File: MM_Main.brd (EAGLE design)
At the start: 101.4 x 83.6 mm, 73 parts, among them IC1 ULN2003AD, IC2 TB6612FNG, IC4 LD117ADT50TR, Q1 TEFT4300, Q2 TEFT4300, Q3 TEFT4300, Q4 TEFT4300, Q7 8MHz, U1 STM32F405RGT6

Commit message: dodalem stm32f4 do biblioteki
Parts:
- removed U$3: STM32F405/415_LQFP64, STM32F10x F4xx:STM32F405/415_LQFP64
- added U$6: STM32F4X5, _microMouse:STM32F4-LQFP64
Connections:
- net +3V3: now also U$6.VDDA, U$6.VDD_0, U$6.VDD_1, U$6.VDD_2, U$6.VDD_3; no longer U$3.VDDA, U$3.VDD_0, U$3.VDD_1, U$3.VDD_2, U$3.VDD_3
- net ADC_L: now also U$6.PC1; no longer U$3.PC1
- net ADC_LF: now also U$6.PC0; no longer U$3.PC0
- net ADC_R: now also U$6.PC2; no longer U$3.PC2
- net ADC_RF: now also U$6.PC3; no longer U$3.PC3
- net ADC_VBAT: now also U$6.PB1; no longer U$3.PB1
- net BOOT0: now also U$6.BOOT0; no longer U$3.BOOT0
- net BTN: now also U$6.PB0; no longer U$3.PB0
- net BT_RXD: now also U$6.PA9; no longer U$3.PA9
- net BT_TXD: now also U$6.PA10; no longer U$3.PA10
- net BUZZER: now also U$6.PA5; no longer U$3.PA5
- net CS_A: now also U$6.PB4; no longer U$3.PB4
- net CS_G: now also U$6.PB3; no longer U$3.PB3
- net D_L: now also U$6.PA2; no longer U$3.PA2
- net D_LF: now also U$6.PA1; no longer U$3.PA1
- net D_LL: now also U$6.PC13; no longer U$3.PC13
- net D_R: now also U$6.PA3; no longer U$3.PA3
- net D_RF: now also U$6.PA4; no longer U$3.PA4
- net D_RR: now also U$6.PC14; no longer U$3.PC14
- net ENCL_A: now also U$6.PA6; no longer U$3.PA6
- net ENCL_B: now also U$6.PA7; no longer U$3.PA7
- net ENCR_A: now also U$6.PB6; no longer U$3.PB6
- net ENCR_B: now also U$6.PB7; no longer U$3.PB7
- net GND: now also U$6.VSS_0, U$6.VSS_1; no longer U$3.VSS_0, U$3.VSS_1
- net GNDA: now also U$6.VSSA; no longer U$3.VSSA
- net INT_A: now also U$6.PB5; no longer U$3.PB5
- net LED1: now also U$6.PB9; no longer U$3.PB9
- net LED2: now also U$6.PB8; no longer U$3.PB8
- net MISO: now also U$6.PC11; no longer U$3.PC11
- net ML_IN1: now also U$6.PC6; no longer U$3.PC6
- net ML_IN2: now also U$6.PC7; no longer U$3.PC7
- net ML_PWM: now also U$6.PB14; no longer U$3.PB14
- net MOSI: now also U$6.PC12; no longer U$3.PC12
- net MR_IN1: now also U$6.PC8; no longer U$3.PC8
- net MR_IN2: now also U$6.PC9; no longer U$3.PC9
- net MR_PWM: now also U$6.PB15; no longer U$3.PB15
- net N$2: now also U$6.PB2; no longer U$3.PB2
- net N$52: now also U$6.PC15; no longer U$3.PC15
- net N$55: now also U$6.PC4; no longer U$3.PC4
- net N$57: now also U$6.PC5; no longer U$3.PC5
- net OSC_IN: now also U$6.PH0; no longer U$3.PH0
- net OSC_OUT: now also U$6.PH1; no longer U$3.PH1
- net RST: now also U$6.NRST; no longer U$3.NRST
- net SCLK: now also U$6.PC10; no longer U$3.PC10
- net SWCLK: now also U$6.PA14; no longer U$3.PA14
- net SWDIO: now also U$6.PA13; no longer U$3.PA13
- net VCAP_1: now also U$6.VCAP_1; no longer U$3.VCAP_1
- net VCAP_2: now also U$6.VCAP_2; no longer U$3.VCAP_2

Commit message: nowe gniazdo do zas
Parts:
- removed BAT, BAT1: (no value), pinhead:1X03
- removed C_V3: 100n, rcl:C0805
- removed SV1: (no value), con-lstb:MA04-2
- removed U$6: STM32F4X5, _microMouse:STM32F4-LQFP64
- removed VCAP_1, VCAP_2: 2,2u, rcl:C0805
- added JP1: (no value), pinhead:2X04
- added JP2: (no value), SparkFun-Connectors:MOLEX-1X3
- R15: device rcl:R0805 -> resistor:R1206W
- moved L2 369.1 mm to (-60.8, -54.8), turned to 315 degrees
- moved L1 279.5 mm to (67.0, 328.3)
- moved R15 45.0 mm to (-115.6, -14.9), turned to 90 degrees
- moved R13 5.05 mm to (4.16, -31.1)
- moved R12 4.57 mm to (13.4, -31.1)
- moved R10 4.41 mm to (9.08, -31.1)
- moved R2 4.30 mm to (0.00, 31.0), turned to 270 degrees
- moved FUSE1 3.76 mm to (-28.9, -21.5), turned to 180 degrees
- moved ZAS 2.59 mm to (-25.7, -24.4), turned to 90 degrees
- moved FUSE 1.99 mm to (-32.3, -22.5)
- moved R9 1.11 mm to (-7.30, -13.0)
- moved C_VSSA 0.97 mm to (-7.46, 20.5), turned to 180 degrees
- moved C6 0.87 mm to (-25.2, 11.8)
- moved R5 0.84 mm to (-24.4, 15.7)
- moved C22 0.81 mm to (-14.1, -28.9)
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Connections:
- removed net N$2: R15.2, U$6.PB2
- removed net N$52: U$6.PC15
- removed net N$55: U$6.PC4
- removed net N$57: U$6.PC5
- removed net VCAP_1: U$6.VCAP_1, VCAP_1.1
- removed net VCAP_2: U$6.VCAP_2, VCAP_2.1
- new net N$20: BOOT.2
- new net N$22: U1.31
- new net N$3: BOOT.3, S1.3
- net +3V3: now also BOOT.1, JP1.7, JP1.8, U1.13, U1.19, U1.32, U1.48, U1.64; no longer C_V3.1, SV1.1, SV1.2, U$6.VDDA, U$6.VDD_0, U$6.VDD_1, U$6.VDD_2, U$6.VDD_3, U1.12, U1.18, U1.63
- net ADC_L: no longer U$6.PC1
- net ADC_LF: no longer U$6.PC0
- net ADC_R: no longer U$6.PC2
- net ADC_RF: no longer U$6.PC3
- net ADC_VBAT: no longer U$6.PB1
- net BOOT0: no longer U$6.BOOT0
- net BTN: no longer U$6.PB0
- net BT_RXD: now also JP1.1; no longer SV1.6, U$6.PA9
- net BT_TXD: now also JP1.3; no longer SV1.8, U$6.PA10
- net BUZZER: no longer U$6.PA5
- net CS_A: no longer U$6.PB4
- net CS_G: no longer U$6.PB3
- net D_L: no longer U$6.PA2
- net D_LF: no longer U$6.PA1
- net D_LL: no longer U$6.PC13
- net D_R: no longer U$6.PA3
- net D_RF: no longer U$6.PA4
- net D_RR: no longer U$6.PC14
- net ENCL_A: no longer U$6.PA6
- net ENCL_B: no longer U$6.PA7
- net ENCR_A: no longer U$6.PB6
- net ENCR_B: no longer U$6.PB7
- net GND: now also JP1.5, JP1.6, U$4.GND_TAB, U1.12, U1.18, U1.63; no longer C_V3.2, R15.1, SV1.3, SV1.4, U$6.VSS_0, U$6.VSS_1, U1.13, U1.19, U1.32, U1.48, U1.64, VCAP_1.2, VCAP_2.2
- net GNDA: now also JP2.1, JP2.3; no longer BAT.1, BAT.3, BAT1.1, BAT1.3, U$6.VSSA
- net INT_A: no longer U$6.PB5
- net LED1: no longer U$6.PB9
- net LED2: no longer U$6.PB8
- net MISO: no longer U$6.PC11
- net ML_IN1: no longer U$6.PC6
- net ML_IN2: no longer U$6.PC7
- net ML_PWM: no longer U$6.PB14
- net MOSI: no longer U$6.PC12
- net MR_IN1: no longer U$6.PC8
- net MR_IN2: no longer U$6.PC9
- net MR_PWM: no longer U$6.PB15
- net N$9: now also JP2.2; no longer BAT.2, BAT1.2
- net OSC_IN: no longer U$6.PH0
- net OSC_OUT: no longer U$6.PH1
- net RST: no longer U$6.NRST
- net SCLK: no longer U$6.PC10
- net SWCLK: now also JP1.2; no longer SV1.7, U$6.PA14
- net SWDIO: now also JP1.4; no longer SV1.5, U$6.PA13
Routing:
- net N$52: track 0.00 -> 723.7 mm
- net N$55: track 0.00 -> 542.5 mm
- net N$53: track 0.00 -> 181.4 mm
- net N$54: track 0.00 -> 180.7 mm
- net +7V: track 87.6 -> 100.6 mm, vias 2 -> 8
- net N$8: track 20.3 -> 28.4 mm, vias 0 -> 2
- net N$16: track 49.6 -> 42.0 mm
- net N$9: track 14.7 -> 7.69 mm
- net N$14: track 71.4 -> 65.8 mm
- net +3V3: track 337.3 -> 342.8 mm, vias 10 -> 11
- net GNDA: track 114.8 -> 110.2 mm
- net N$17: track 3.94 -> 8.35 mm
- net N$21: track 24.2 -> 27.6 mm, vias 0 -> 2
- net N$19: track 63.2 -> 60.5 mm
- net +5V: track 198.2 -> 200.3 mm
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- added copper zone on layer 1, net GND
- added copper zone on layer 16, net GND
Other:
- board size 101.4 x 83.6 mm -> 101.4 x 83.3 mm

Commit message: dodalem adxrs620
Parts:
- removed JP1: (no value), pinhead:2X04
- removed JP2: (no value), SparkFun-Connectors:MOLEX-1X3
- added BAT, BAT1: (no value), pinhead:1X03
- added C_V3: 100n, rcl:C0805
- added SV1: (no value), con-lstb:MA04-2
- added U$6: STM32F4X5, _microMouse:STM32F4-LQFP64
- added VCAP_1, VCAP_2: 2,2u, rcl:C0805
- R15: device resistor:R1206W -> rcl:R0805
- moved L2 369.1 mm to (-397.5, 96.5), turned to 0 degrees
- moved L1 279.5 mm to (136.7, 57.6)
- moved R15 45.0 mm to (-117.3, 30.0), turned to 0 degrees
- moved R13 5.05 mm to (9.21, -31.1)
- moved R12 4.57 mm to (17.9, -31.1)
- moved R10 4.41 mm to (13.5, -31.1)
- moved R2 4.30 mm to (0.32, 35.2), turned to 0 degrees
- moved FUSE1 3.76 mm to (-32.5, -22.5), turned to 90 degrees
- moved ZAS 2.59 mm to (-27.3, -22.4), turned to 0 degrees
- moved FUSE 1.99 mm to (-30.3, -22.5)
- moved R9 1.11 mm to (-7.30, -14.1)
- moved C_VSSA 0.97 mm to (-7.30, 21.4), turned to 0 degrees
- moved C6 0.87 mm to (-26.0, 11.6)
- moved R5 0.84 mm to (-25.2, 15.7)
- moved C22 0.81 mm to (-14.9, -28.9)
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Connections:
- removed net N$20: BOOT.2
- removed net N$22: U1.31
- removed net N$3: BOOT.3, S1.3
- new net N$2: R15.2, U$6.PB2
- new net N$52: U$6.PC15
- new net N$55: U$6.PC4
- new net N$57: U$6.PC5
- new net VCAP_1: U$6.VCAP_1, VCAP_1.1
- new net VCAP_2: U$6.VCAP_2, VCAP_2.1
- net +3V3: now also C_V3.1, SV1.1, SV1.2, U$6.VDDA, U$6.VDD_0, U$6.VDD_1, U$6.VDD_2, U$6.VDD_3, U1.12, U1.18, U1.63; no longer BOOT.1, JP1.7, JP1.8, U1.13, U1.19, U1.32, U1.48, U1.64
- net ADC_L: now also U$6.PC1
- net ADC_LF: now also U$6.PC0
- net ADC_R: now also U$6.PC2
- net ADC_RF: now also U$6.PC3
- net ADC_VBAT: now also U$6.PB1
- net BOOT0: now also U$6.BOOT0
- net BTN: now also U$6.PB0
- net BT_RXD: now also SV1.6, U$6.PA9; no longer JP1.1
- net BT_TXD: now also SV1.8, U$6.PA10; no longer JP1.3
- net BUZZER: now also U$6.PA5
- net CS_A: now also U$6.PB4
- net CS_G: now also U$6.PB3
- net D_L: now also U$6.PA2
- net D_LF: now also U$6.PA1
- net D_LL: now also U$6.PC13
- net D_R: now also U$6.PA3
- net D_RF: now also U$6.PA4
- net D_RR: now also U$6.PC14
- net ENCL_A: now also U$6.PA6
- net ENCL_B: now also U$6.PA7
- net ENCR_A: now also U$6.PB6
- net ENCR_B: now also U$6.PB7
- net GND: now also C_V3.2, R15.1, SV1.3, SV1.4, U$6.VSS_0, U$6.VSS_1, U1.13, U1.19, U1.32, U1.48, U1.64, VCAP_1.2, VCAP_2.2; no longer JP1.5, JP1.6, U$4.GND_TAB, U1.12, U1.18, U1.63
- net GNDA: now also BAT.1, BAT.3, BAT1.1, BAT1.3, U$6.VSSA; no longer JP2.1, JP2.3
- net INT_A: now also U$6.PB5
- net LED1: now also U$6.PB9
- net LED2: now also U$6.PB8
- net MISO: now also U$6.PC11
- net ML_IN1: now also U$6.PC6
- net ML_IN2: now also U$6.PC7
- net ML_PWM: now also U$6.PB14
- net MOSI: now also U$6.PC12
- net MR_IN1: now also U$6.PC8
- net MR_IN2: now also U$6.PC9
- net MR_PWM: now also U$6.PB15
- net N$9: now also BAT.2, BAT1.2; no longer JP2.2
- net OSC_IN: now also U$6.PH0
- net OSC_OUT: now also U$6.PH1
- net RST: now also U$6.NRST
- net SCLK: now also U$6.PC10
- net SWCLK: now also SV1.7, U$6.PA14; no longer JP1.2
- net SWDIO: now also SV1.5, U$6.PA13; no longer JP1.4
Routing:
- net N$52: track 723.7 -> 0.00 mm
- net N$55: track 542.5 -> 0.00 mm
- net N$53: track 181.4 -> 0.00 mm
- net N$54: track 180.7 -> 0.00 mm
- net +7V: track 100.6 -> 87.6 mm, vias 8 -> 2
- net N$8: track 28.4 -> 20.3 mm, vias 2 -> 0
- net N$16: track 42.0 -> 49.6 mm
- net N$9: track 7.69 -> 14.7 mm
- net N$14: track 65.8 -> 71.4 mm
- net +3V3: track 342.8 -> 337.3 mm, vias 11 -> 10
- net GNDA: track 110.2 -> 114.8 mm
- net N$17: track 8.35 -> 3.94 mm
- net N$21: track 27.6 -> 24.2 mm, vias 2 -> 0
- net N$19: track 60.5 -> 63.2 mm
- net +5V: track 200.3 -> 198.2 mm
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- removed copper zone on layer 1, net GND
- removed copper zone on layer 16, net GND
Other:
- board size 101.4 x 83.3 mm -> 101.4 x 83.6 mm

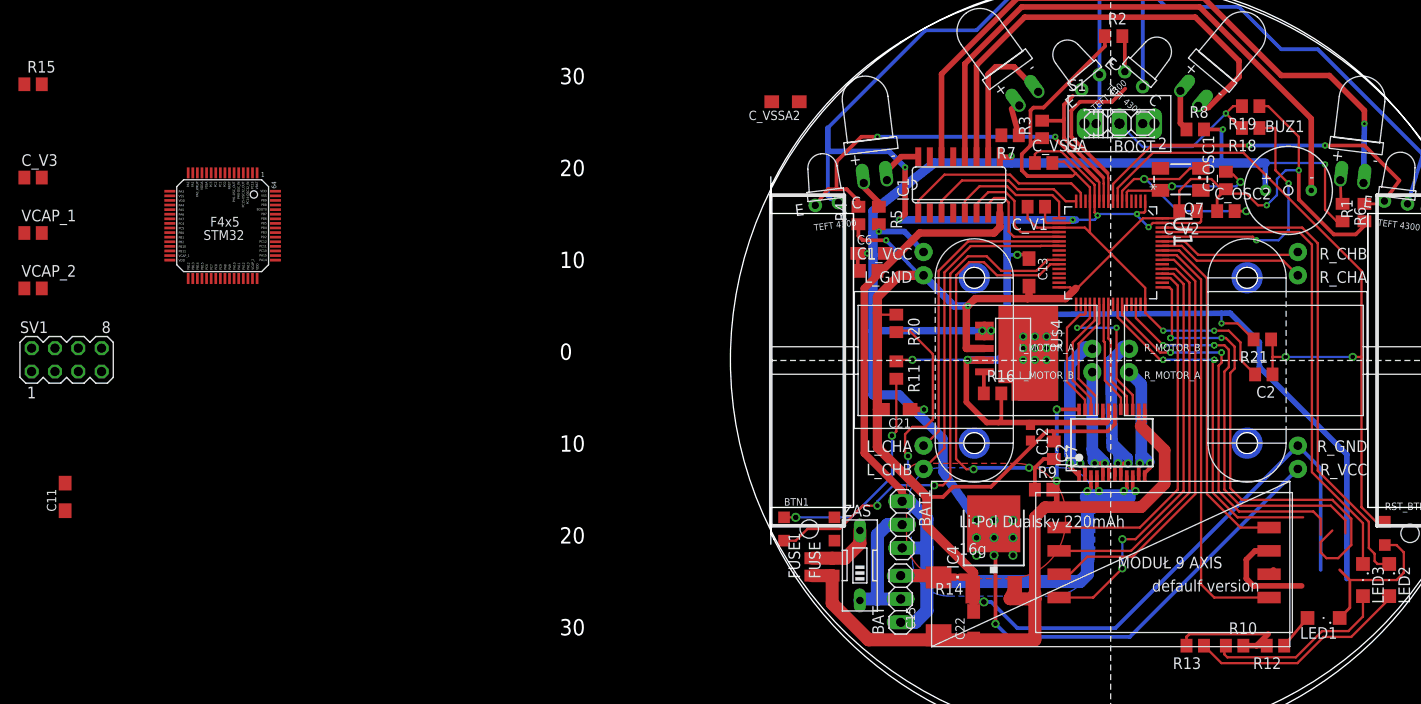
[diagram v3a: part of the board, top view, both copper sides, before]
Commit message: zmiana gniazda zasilania, VCC i VSS
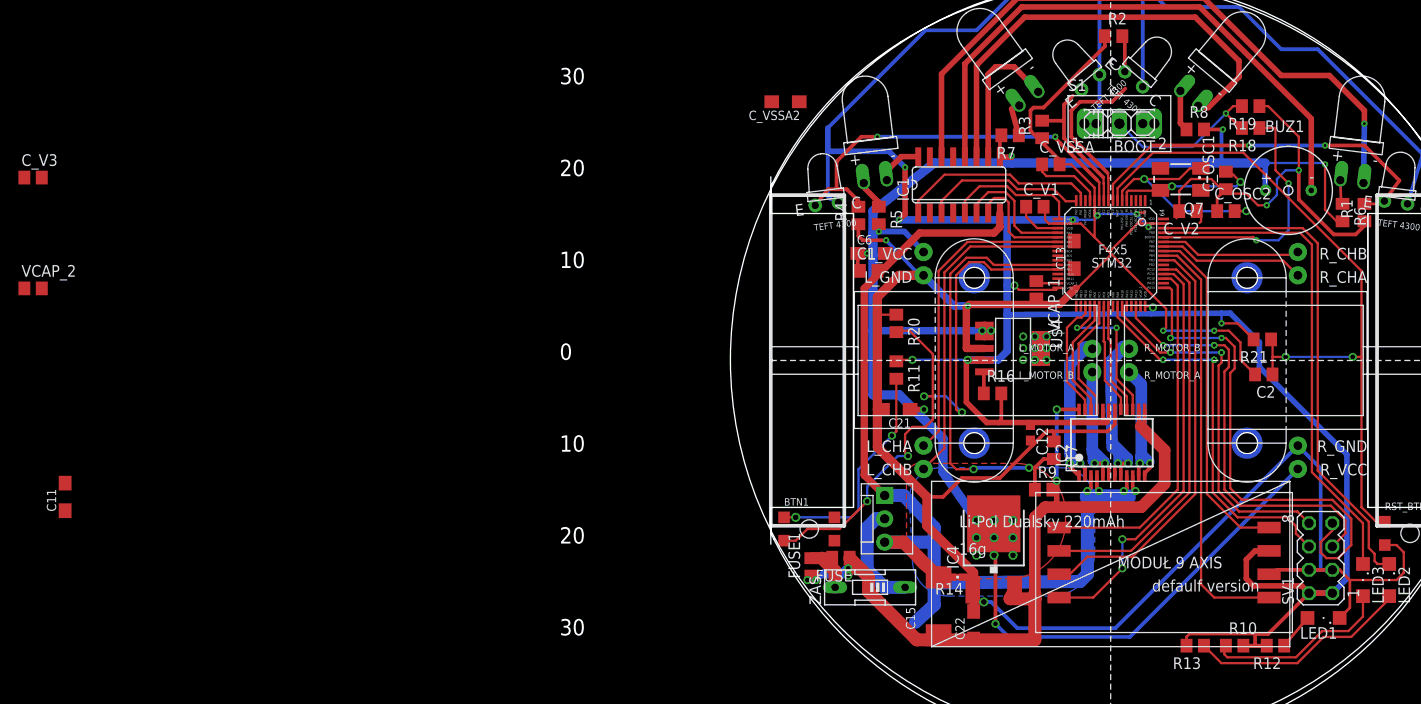
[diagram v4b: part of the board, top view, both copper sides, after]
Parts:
- removed BAT, BAT1: (no value), pinhead:1X03
- removed R15: (no value), rcl:R0805
- removed U1: STM32F405RGT6, _microMouse:QFP50P1200X1200X160-64N
- added JP1: (no value), SparkFun-Connectors:MOLEX-1X3
- moved SV1 138.2 mm to (22.9, -21.6), turned to 90 degrees
- moved VCAP_1 109.4 mm to (-8.10, 7.62), turned to 270 degrees
- moved U$6 96.7 mm to (0.00, 11.6)
- moved C13 5.28 mm to (-3.97, 11.4), turned to 90 degrees
- moved ZAS 2.63 mm to (-26.2, -24.8), turned to 90 degrees
- moved FUSE 1.35 mm to (-29.4, -21.6), turned to 180 degrees
- moved C_VSSA 0.81 mm to (-6.51, 21.3)
- moved C_V1 0.16 mm to (-8.26, 16.7), turned to 0 degrees
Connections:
- removed net N$2: R15.2, U$6.PB2
- removed net N$30: U1.41
- removed net N$32: U1.47
- removed net N$34: U1.50
- removed net N$35: U1.54
- removed net N$38: U1.34
- removed net N$39: U1.33
- removed net N$40: U1.24
- removed net N$41: U1.25
- removed net N$42: U1.30
- net +3V3: no longer U1.1, U1.12, U1.18, U1.63
- net ADC_L: no longer U1.9
- net ADC_LF: no longer U1.8
- net ADC_R: no longer U1.10
- net ADC_RF: no longer U1.11
- net ADC_VBAT: no longer U1.27
- net BOOT0: no longer U1.60
- net BTN: now also U$6.PB2; no longer U$6.PB0, U1.26
- net BT_RXD: no longer U1.42
- net BT_TXD: no longer U1.43
- net BUZZER: no longer U1.21
- net CS_A: no longer U1.56
- net CS_G: no longer U1.55
- net D_L: no longer U1.16
- net D_LF: no longer U1.15
- net D_LL: no longer U1.2
- net D_R: no longer U1.17
- net D_RF: no longer U1.20
- net D_RR: no longer U1.3
- net ENCL_A: no longer U1.22
- net ENCL_B: no longer U1.23
- net ENCR_A: no longer U1.58
- net ENCR_B: no longer U1.59
- net GND: now also U$4.GND_TAB, U$6.VSSA; no longer R15.1, U1.13, U1.19, U1.32, U1.48, U1.64
- net GNDA: now also JP1.1, JP1.3; no longer BAT.1, BAT.3, BAT1.1, BAT1.3, U$6.VSSA
- net INT_A: no longer U1.57
- net LED1: no longer U1.62
- net LED2: no longer U1.61
- net MISO: no longer U1.52
- net ML_IN1: no longer U1.37
- net ML_IN2: no longer U1.38
- net ML_PWM: no longer U1.35
- net MOSI: no longer U1.53
- net MR_IN1: no longer U1.39
- net MR_IN2: no longer U1.40
- net MR_PWM: no longer U1.36
- net N$9: now also JP1.2; no longer BAT.2, BAT1.2
- net OSC_IN: no longer U1.5
- net OSC_OUT: no longer U1.6
- net RST: no longer U1.7
- net SCLK: no longer U1.51
- net SWCLK: no longer U1.49
- net SWDIO: no longer U1.46
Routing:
- net +3V3: track 337.3 -> 347.4 mm, vias 10 -> 11
- net +7V: track 87.6 -> 96.6 mm, vias 2 -> 6
- net BTN: track 78.9 -> 70.1 mm, vias 3 -> 4
- net BT_TXD: track 43.0 -> 39.9 mm
- net N$9: track 14.7 -> 11.8 mm
- net VCAP_1: track 0.00 -> 2.39 mm
- net +5V: track 198.2 -> 200.5 mm
- net GNDA: track 114.8 -> 117.2 mm
- net GND: track 326.9 -> 324.7 mm
- net BT_RXD: track 39.3 -> 41.5 mm
- net SWDIO: track 44.4 -> 46.3 mm
- net N$24: track 7.33 -> 5.99 mm
- net ADC_VBAT: track 46.9 -> 47.9 mm
- net SWCLK: track 54.1 -> 54.7 mm

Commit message: no male dodatki
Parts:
- removed BOOT: (no value), pinhead:1X03
- removed S1: (no value), switch:255SB
- added BTN2: TACTILE-SWITCH-7914G, GeekAmmo:7914G
- moved C13 0.35 mm to (-3.81, 11.1)
- turned C_V2 to 0 degrees
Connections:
- net +3V3: now also BTN2.3; no longer S1.1
- net BOOT0: now also U$6.PD2
- net N$23: now also BTN2.1; no longer S1.2
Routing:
- net BOOT0: track 28.2 -> 33.1 mm
- net GND: track 324.7 -> 322.8 mm
- net N$23: track 18.6 -> 19.8 mm, vias 1 -> 2
- net BTN: track 70.1 -> 70.6 mm
- net ADC_VBAT: track 47.9 -> 48.4 mm
- net +3V3: track 347.4 -> 347.9 mm, vias 11 -> 10

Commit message: rozwoj pcb
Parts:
- moved L2 409.1 mm to (0.00, -0.16)
- moved L1 333.9 mm to (470.5, 57.0)
- moved VCAP_2 121.7 mm to (4.29, 2.54), turned to 270 degrees
- moved C13 42.8 mm to (-46.2, 5.40)
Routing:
- net +3V3: track 347.9 -> 351.7 mm
- net VCAP_2: track 0.00 -> 2.78 mm
- net GND: track 322.8 -> 325.1 mm
- net N$21: track 24.2 -> 26.4 mm, vias 0 -> 2
- net N$8: track 20.3 -> 18.5 mm, vias 0 -> 2
- net BT_RXD: track 41.5 -> 42.2 mm
- net BT_TXD: track 39.9 -> 40.5 mm
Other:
- board size 101.4 x 83.6 mm -> 101.4 x 81.1 mm

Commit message: poczatek 6LED -- dlugi przod
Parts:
- added D5, D6: SFH4545-C, _microMouse:SFH4545-C
- added Q5, Q6: TEFT4300, _MM:TEFT4300
- added R15, R22, R23, R24: (no value), rcl:R0805
- moved C_V1 0.71 mm to (-7.94, 16.0), turned to 90 degrees
- moved Q7 0.16 mm to (7.62, 19.5)
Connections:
- removed net N$52: U$6.PC15
- removed net N$55: U$6.PC4
- removed net N$57: U$6.PC5
- new net +5V1: R15.2
- new net N$2: D5.KATODA, IC1.15
- new net N$20: D6.ANODA, R22.1
- new net N$22: D6.KATODA, IC1.13
- new net N$25: Q5.E, R23.2
- new net N$3: D5.ANODA, R15.1
- new net N$31: Q6.E, R24.2
- net +3V3: now also Q5.C, Q6.C, U$6.VBAT
- net +5V: now also R22.2
- net BUZZER: now also U$6.PC5; no longer U$6.PA5
- net D_L: now also U$6.PA1; no longer U$6.PA2
- net D_LF: now also U$6.PC15; no longer U$6.PA1
- net D_LL: now also IC1.4
- net D_R: now also U$6.PA5; no longer U$6.PA3
- net D_RF: now also U$6.PC4; no longer U$6.PA4
- net D_RR: now also IC1.2
- net GND: now also R23.1, R24.1
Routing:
- net D_RR: track 0.00 -> 28.6 mm, vias 0 -> 2
- net D_LL: track 0.00 -> 25.2 mm, vias 0 -> 2
- net D_LF: track 21.9 -> 29.5 mm, vias 0 -> 2
- net OSC_IN: track 15.8 -> 20.4 mm
- net OSC_OUT: track 24.6 -> 28.2 mm
- net BUZZER: track 12.8 -> 15.8 mm, vias 0 -> 2
- net D_RF: track 13.8 -> 16.3 mm, vias 0 -> 2
- net D_L: track 17.9 -> 19.9 mm, vias 0 -> 2
- net RST: track 77.3 -> 79.1 mm
- net ADC_LF: track 41.5 -> 43.2 mm
- net +3V3: track 351.7 -> 352.9 mm
- net D_R: track 15.6 -> 16.6 mm
- net GND: track 325.1 -> 326.0 mm

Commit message: zmieniony przod i kolejnosc ledow
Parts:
- removed C_VSSA2: tant-a-4,7u, rcl:SMC_A
- added C_VSSA1: 100n, rcl:C0805
- moved R24 593.2 mm to (-121.0, -31.0)
- moved Q6 591.0 mm to (-122.0, -25.0)
- moved R23 582.0 mm to (-129.0, -32.0)
- moved Q5 581.4 mm to (-129.0, -25.0)
- moved D6 571.0 mm to (-150.0, -28.0)
- moved R22 320.8 mm to (-150.0, -32.0)
- moved D5 319.9 mm to (-137.4, -27.4)
- moved C_V3 82.1 mm to (-35.8, 9.68), turned to 90 degrees
- moved C11 70.0 mm to (-44.8, -2.92)
- moved R15 68.6 mm to (-137.0, -32.0)
- moved D2 55.0 mm to (-28.6, 22.2), turned to 7 degrees
- moved D1 54.7 mm to (29.0, 22.2), turned to 353 degrees
- moved R5 50.6 mm to (25.2, 18.9), turned to 180 degrees
- moved R6 50.4 mm to (-25.1, 19.6), turned to 0 degrees
- moved BUZ1 36.3 mm to (-13.6, 33.6), turned to 180 degrees
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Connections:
- removed net N$22: D6.KATODA, IC1.13
- net +3V3: now also C_VSSA1.1; no longer C_VSSA2.+
- net GND: now also C_VSSA1.2; no longer C_VSSA2.-
- net N$13: now also D2.KATODA; no longer D1.KATODA
- net N$14: now also D1.KATODA, IC1.10; no longer D2.KATODA, IC1.14
- net N$15: now also IC1.12; no longer IC1.10
- net N$19: now also IC1.13; no longer IC1.12
- net N$2: no longer IC1.15
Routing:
- net N$19: track 63.2 -> 11.9 mm
- net +3V3: track 352.9 -> 306.8 mm
- net +5V: track 200.5 -> 230.6 mm, vias 18 -> 20
- net GND: track 326.0 -> 348.2 mm, vias 7 -> 13
- net ADC_R: track 16.4 -> 36.9 mm, vias 0 -> 2
- net N$15: track 15.9 -> 34.6 mm
- net N$14: track 71.4 -> 54.2 mm
- net ADC_L: track 22.3 -> 36.0 mm, vias 0 -> 2
- net N$16: track 49.6 -> 35.9 mm
- net ADC_RF: track 43.8 -> 32.5 mm
- net ADC_LF: track 43.2 -> 34.1 mm
- net N$23: track 19.8 -> 15.0 mm, vias 2 -> 1
- net N$13: track 4.17 -> 6.51 mm
- net N$10: track 2.65 -> 4.51 mm
- net N$12: track 4.48 -> 5.53 mm
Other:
- board size 101.4 x 81.1 mm -> 287.5 x 95 mm
